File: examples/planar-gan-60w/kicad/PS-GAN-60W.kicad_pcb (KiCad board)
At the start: 8 copper layers, 80 x 58 mm, 89 parts, among them J1 XT30 48V INPUT, J2 XT30 12V OUTPUT, Q1 CSD18543Q3A, Q2 CSD18543Q3A, T1 4:2:2 / Lm 13.12uH, U1 LMG2100R044RARR, U2 UCC25600DR, U3 UCC24624DR, U4 LM5164DDAR, U5 TPS7A2450DBVR, U6 EL357N(A)(TA)-VG, U7 TL431AIDBZR, U8 EL357N(A)(TA)-VG, U9 TL431AIDBZR

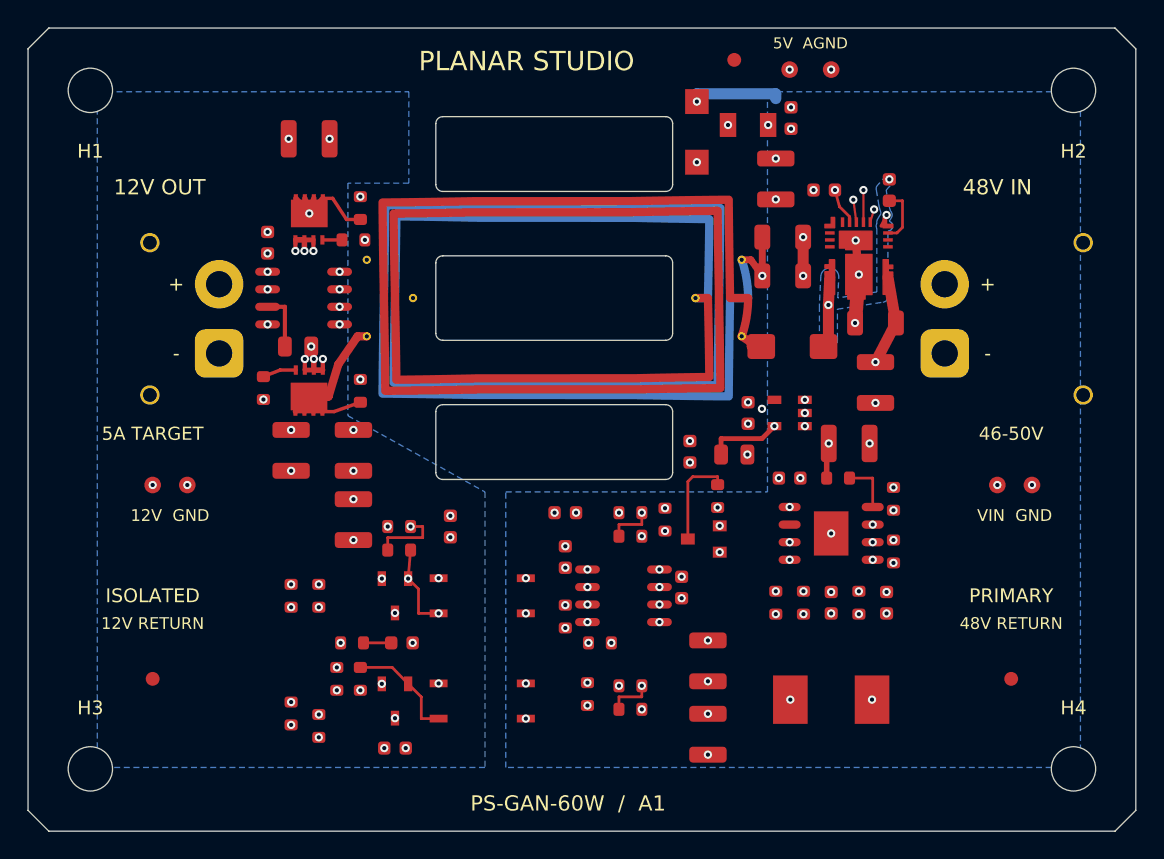
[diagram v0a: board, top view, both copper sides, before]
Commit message: Redraw GaN schematic and compact the bench-accessible A2 board
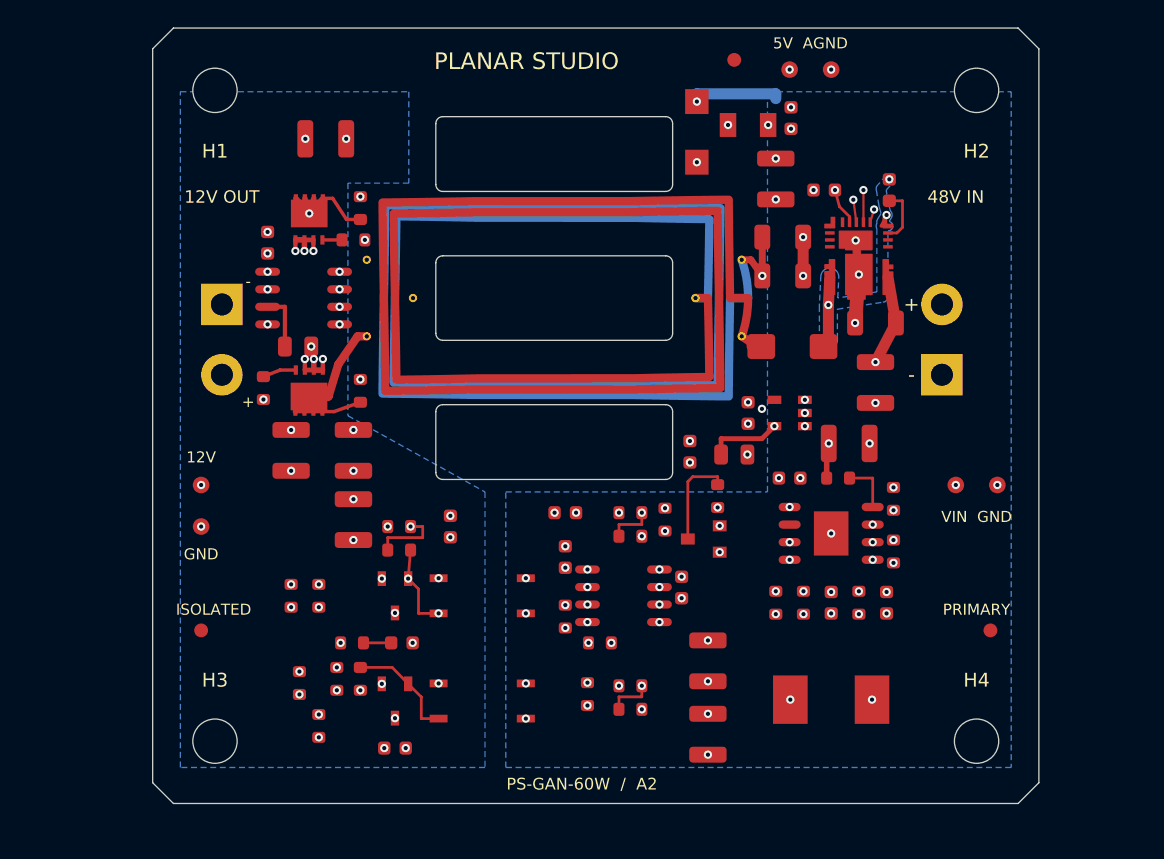
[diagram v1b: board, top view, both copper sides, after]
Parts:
- C7, C8: value 100nF/100V C0G -> 100nF/100V
- D2: value BAT54SLT1G -> BAT54S
- J1: value XT30 48V INPUT -> 48 V INPUT; footprint PS:AMASS_XT30PW-M_1x02_P2.50mm_Horizontal -> PS:CONN-TH_2P-P5.08_WJ2EDGRC-5.08-2P
- J2: value XT30 12V OUTPUT -> 12 V / 5 A; footprint PS:AMASS_XT30PW-F_1x02_P2.50mm_Horizontal -> PS:CONN-TH_2P-P5.08_WJ2EDGRC-5.08-2P
- T1: value 4:2:2 / Lm 13.12uH -> 4 : 2 : 2 / ELP22
- U1: value LMG2100R044RARR -> LMG2100R044
- U2: value UCC25600DR -> UCC25600
- U3: value UCC24624DR -> UCC24624
- U4: value LM5164DDAR -> LM5164
- U5: value TPS7A2450DBVR -> TPS7A2450
- U6, U8: value EL357N(A)(TA)-VG -> EL357N
- U7, U9: value TL431AIDBZR -> TL431A
- moved H3 9.22 mm to (57.5, 107.5)
- moved H1 9.00 mm to (57.5, 60.5)
- moved H4 7.28 mm to (112.5, 107.5)
- moved H2 7.00 mm to (112.5, 60.5)
- moved FID1 4.95 mm to (56.5, 99.5)
- moved FID2 3.81 mm to (113.5, 99.5)
- moved TP3 3.50 mm to (56.5, 89.0)
- moved TP4 3.16 mm to (56.5, 92.0)
- moved TP1 3.00 mm to (111.0, 89.0)
- moved TP2 2.50 mm to (114.0, 89.0)
- moved R27 2.28 mm to (63.6, 103.3)
- moved C15 1.20 mm to (65.5, 64.0)
- moved J1 1.02 mm to (110.0, 78.5), turned to 90 degrees
- moved J2 1.02 mm to (58.0, 78.5), turned to -90 degrees
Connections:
- net /AGND renamed AGND
- net /BIAS12 renamed BIAS12
- net /PGND renamed PGND
- net /SGND renamed SGND
- net /V5 renamed V5
- net /VIN renamed VIN
- net /VOUT renamed VOUT
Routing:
- net VIN: track 103.3 -> 99.7 mm
- net VOUT: track 130.5 -> 128.2 mm
- net /OV_REF: track 17.7 -> 18.3 mm
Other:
- board size 80 x 58 mm -> 64 x 56 mm
- board text added: "12V"
- board text added: "GND"
- board text added: "PS-GAN-60W / A2"
- board text removed: "12V GND"
- board text removed: "12V RETURN"
- board text removed: "46-50V"
- board text removed: "48V RETURN"
- board text removed: "5A TARGET"
- board text removed: "PS-GAN-60W / A1"

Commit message: Improve GaN example schematic spacing and readability
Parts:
- C1, C19, C2: value 2.2uF/100V -> 2.2uF
- C10, C12, C25, C5: value 1uF/25V -> 1uF
- C11, C26: value 2.2uF/25V -> 2.2uF
- C13, C14, C15, C16, C21, C22: value 22uF/25V -> 22uF
- C17, C18, C27, C29: value 10nF/50V -> 10nF
- C20: value 2.2nF/50V -> 2.2nF
- C23: value 3.3nF/50V -> 3.3nF
- C24: value 56pF/50V -> 56pF
- C28: value 1nF/50V -> 1nF
- C3: value 100nF/100V C0G -> 100nF
- C4, C6, C9: value 100nF/50V -> 100nF
- C7, C8: value 100nF/100V -> 100nF
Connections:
- net /BIAS_BST renamed Net-(U4-BST)
- net /BIAS_EN renamed Net-(U4-EN/UVLO)
- net /COMP renamed Net-(C27-Pad1)
- net /CS_AC renamed Net-(C17-Pad2)
- net /CS_RECT renamed Net-(D2-A/C)
- net /DT renamed Net-(U2-DT)
- net /FB_K renamed Net-(U6-CA)
- net /FB_LED renamed Net-(U6-AN)
- net /GD1 renamed Net-(U2-GD1)
- net /GD2 renamed Net-(U2-GD2)
- net /HB renamed Net-(U1-HB)
- net /OV_K renamed Net-(U8-CA)
- net /OV_LED renamed Net-(U8-AN)
- net /OV_REF renamed Net-(U9-REF)
- net /PRI_A renamed Net-(T1-P_DOT)
- net /RIPPLE renamed Net-(C23-Pad1)
- net /RON renamed Net-(U4-RON)
- net /RT renamed Net-(U2-RT)
- net /SR_G1 renamed Net-(Q1-G)
- net /SR_G2 renamed Net-(Q2-G)
- net /SR_REG renamed Net-(U3-REG)
- net /VG1 renamed Net-(U3-VG1)
- net /VG2 renamed Net-(U3-VG2)
- net /VREF renamed Net-(U7-REF)
- net /VS1 renamed Net-(U3-VD1)
- net /VS2 renamed Net-(U3-VD2)

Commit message: Wire sense and bias circuits cohesively in GaN schematic
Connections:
- net /BIAS_FB renamed Net-(U4-FB)
- net /BIAS_SW renamed Net-(U4-SW)
- net /OC renamed Net-(D2-C)
- net /SEC_A renamed Net-(T1-S_DOT)
- net /SEC_B renamed Net-(T1-S_END)

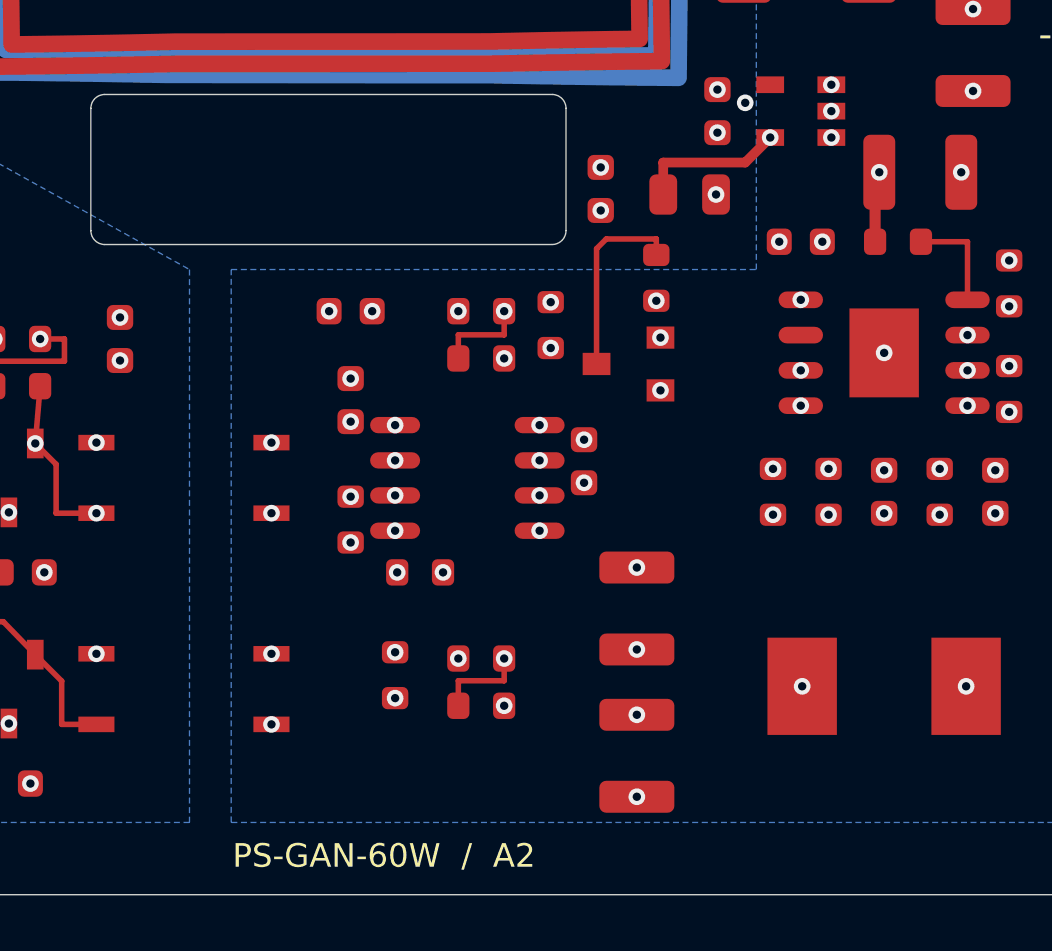
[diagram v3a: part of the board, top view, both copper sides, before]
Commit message: Clarify GaN schematic and correct LM5164 RON grounding
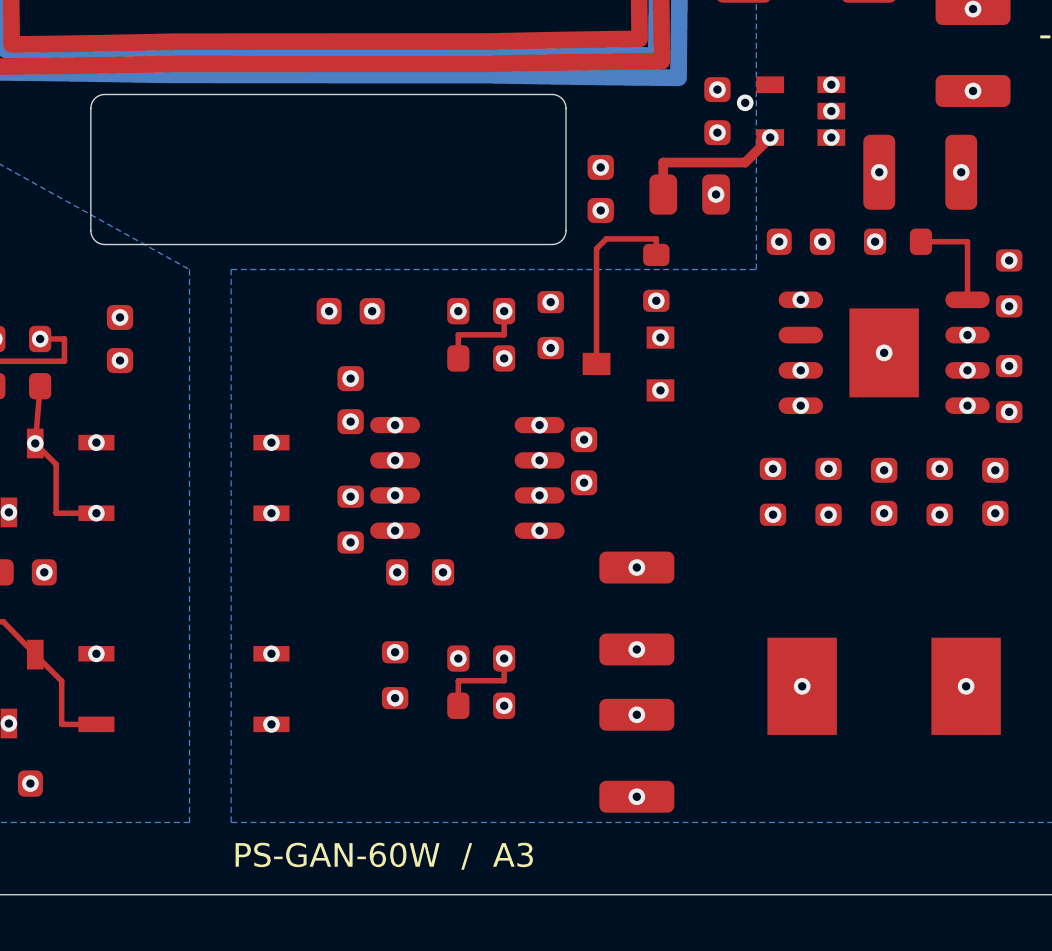
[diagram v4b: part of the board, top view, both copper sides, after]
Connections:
- R16 pad 1: VIN -> PGND
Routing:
- net VIN: track 99.7 -> 97.2 mm
- net PGND: vias 16 -> 17
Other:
- board text added: "PS-GAN-60W / A3"
- board text removed: "PS-GAN-60W / A2"

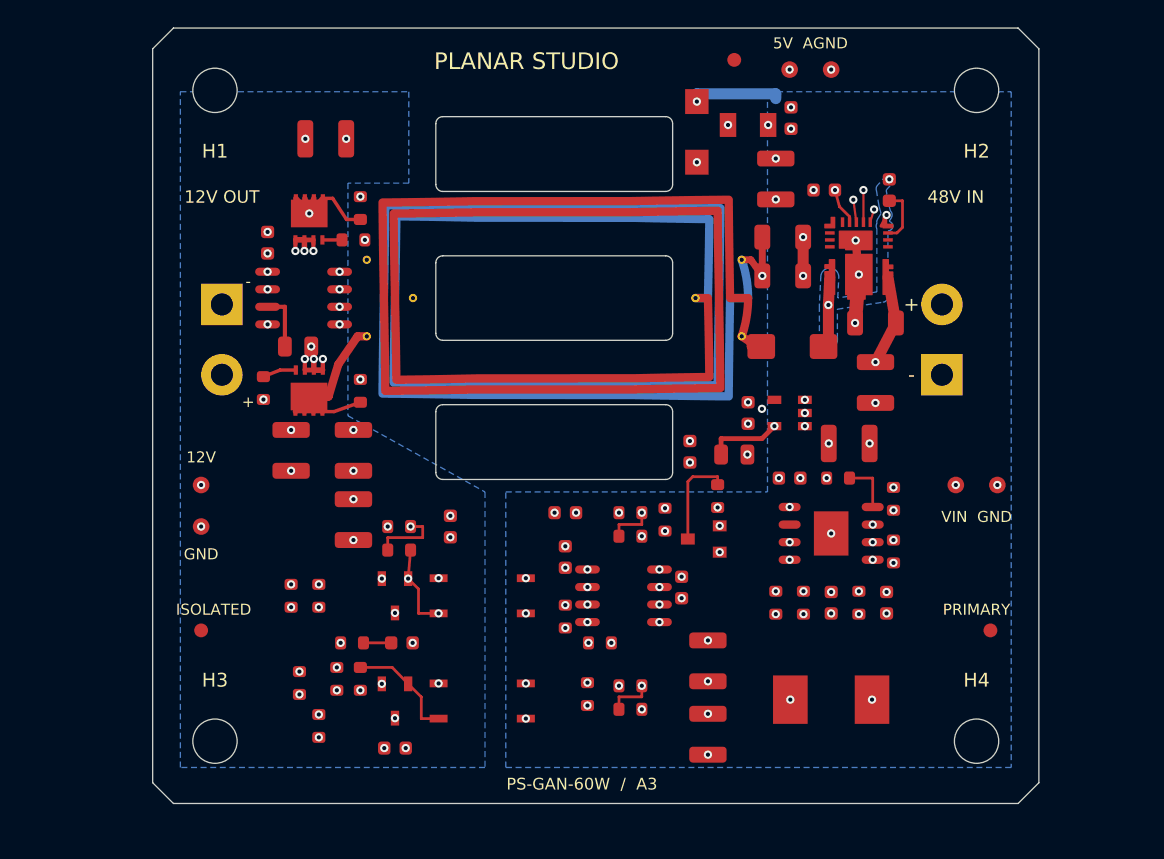
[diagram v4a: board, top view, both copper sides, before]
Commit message: Tighten GaN switching loops and separate rectifier sense return
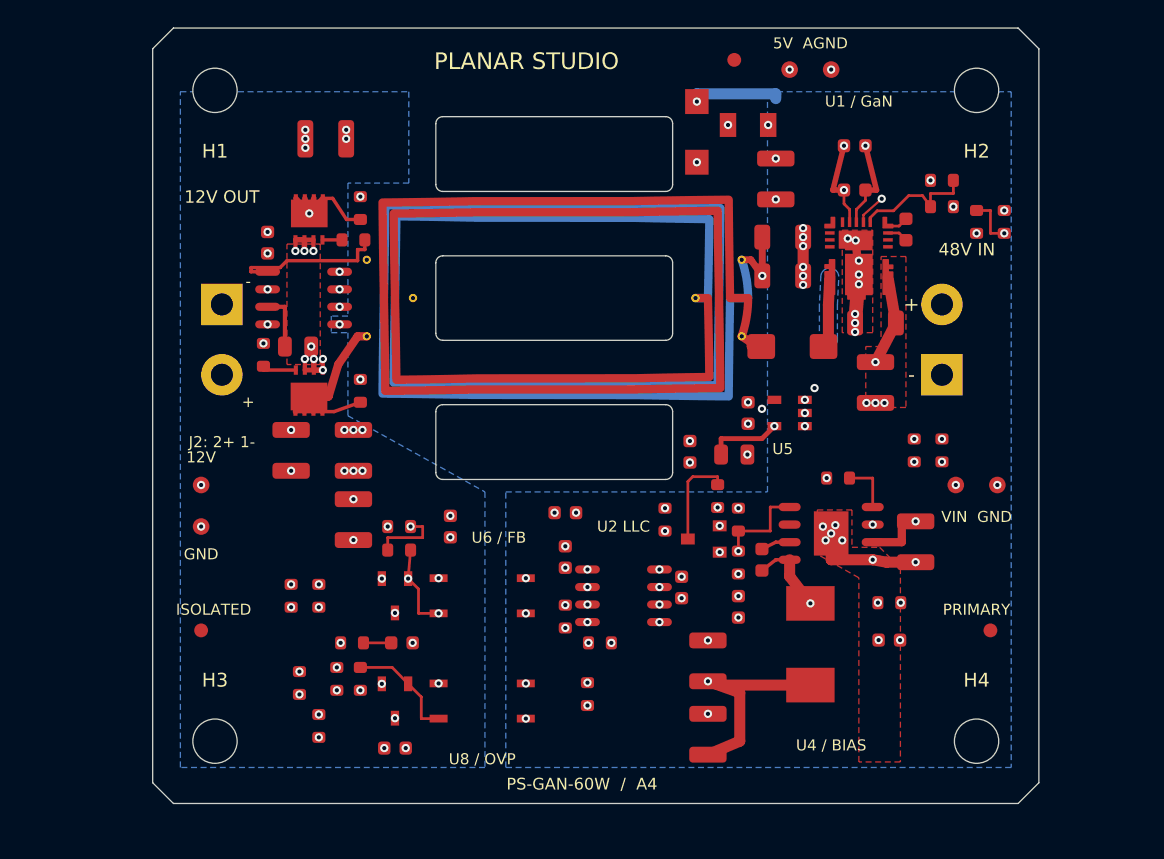
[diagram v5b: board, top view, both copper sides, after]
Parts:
- moved R7 44.4 mm to (114.5, 70.0), turned to 90 degrees
- moved R6 41.8 mm to (112.5, 70.0), turned to 90 degrees
- moved R4 32.9 mm to (110.0, 67.0)
- moved R5 32.8 mm to (110.0, 68.9)
- moved C19 8.57 mm to (108.1, 93.1), turned to -90 degrees
- moved R15 8.10 mm to (110.0, 86.5)
- moved C24 6.71 mm to (95.3, 97.8)
- moved R17 6.58 mm to (95.3, 91.5), turned to -90 degrees
- moved C20 6.23 mm to (97.0, 94.4), turned to -90 degrees
- moved R18 5.52 mm to (95.3, 94.6), turned to -90 degrees
- moved C5 5.02 mm to (103.7, 64.5), turned to 180 degrees
- moved L2 4.27 mm to (100.5, 100.5), turned to -90 degrees
- moved R14 3.81 mm to (108.0, 86.5)
- moved C4 3.09 mm to (107.4, 70.5)
- moved C23 2.71 mm to (106.2, 100.2), turned to 0 degrees
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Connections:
- C4 pad 2: /SW -> Net-(U1-HS)
- U1 pad 11: /SW -> Net-(U1-HS)
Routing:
- net Net-(U2-GD1): track 7.02 -> 55.9 mm
- net Net-(U2-GD2): track 8.37 -> 49.4 mm
- net /LI: track 54.8 -> 19.5 mm
- net /HI: track 41.5 -> 9.30 mm, vias 2 -> 0
- net PGND: track 15.4 -> 34.8 mm, vias 17 -> 32
- net Net-(U4-SW): track 29.6 -> 11.0 mm, vias 4 -> 2
- net /SW: track 19.3 -> 5.13 mm, vias 3 -> 0
- net AGND: track 52.0 -> 62.9 mm
- net /VIN_RAW: track 29.9 -> 40.0 mm
- net Net-(C23-Pad1): track 6.96 -> 16.4 mm
- net VIN: track 97.2 -> 89.9 mm, vias 8 -> 7
- net BIAS12: track 78.5 -> 85.3 mm, vias 10 -> 8
- net SGND: track 10.3 -> 16.5 mm, vias 20 -> 24
- net V5: track 47.7 -> 53.8 mm, vias 5 -> 4
- net Net-(U4-FB): track 16.1 -> 10.8 mm, vias 4 -> 2
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- added copper zone on In1.Cu, net AGND
- added copper zone on F.Cu, net PGND
- added copper zone on F.Cu, net SGND
- added copper zone on In1.Cu, net SGND
- added copper zone on F.Cu, net VIN
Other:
- board text added: "J2: 2+ 1-"
- board text added: "PS-GAN-60W / A4"
- board text added: "U1 / GaN"
- board text added: "U2 LLC"
- board text added: "U4 / BIAS"
- board text added: "U5"
- board text added: "U6 / FB"
- board text added: "U8 / OVP"
- board text removed: "PS-GAN-60W / A3"

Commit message: Refine GaN example return paths and rectifier placement
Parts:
- C10: footprint PS:C_0603_1608Metric -> PS:C_0805_2012Metric
- moved R7 14.6 mm to (99.9, 69.8), turned to 0 degrees
- moved R6 12.8 mm to (99.9, 68.0), turned to 0 degrees
- moved C12 9.27 mm to (64.5, 80.2), turned to 0 degrees
- moved C11 8.19 mm to (61.0, 71.2), turned to 180 degrees
- moved C25 6.54 mm to (102.5, 84.5)
- moved C26 2.75 mm to (96.5, 84.5), turned to 180 degrees
- moved C1 2.72 mm to (99.6, 64.7)
- moved C15 1.40 mm to (65.5, 65.4)
- moved C13 1.20 mm to (63.0, 87.7)
- moved C14 1.20 mm to (67.5, 87.7)
- moved C16 1.20 mm to (67.5, 92.7)
- moved C7 1.12 mm to (98.7, 72.2)
- moved C8 1.12 mm to (98.7, 75.0)
- moved R10 1.08 mm to (66.9, 72.2), turned to 90 degrees
- moved Q2 1.00 mm to (64.3, 83.2)
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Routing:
- net AGND: track 62.9 -> 30.1 mm, vias 19 -> 18
- net Net-(U3-VG1): track 11.4 -> 1.11 mm
- net Net-(U2-GD1): track 55.9 -> 45.9 mm
- net Net-(U2-GD2): track 49.4 -> 40.0 mm
- net Net-(U3-VD1): track 17.1 -> 11.0 mm
- net Net-(U3-VG2): track 11.7 -> 6.08 mm
- net V5: track 53.8 -> 48.5 mm
- net VIN: track 89.9 -> 84.7 mm
- net /LI: track 19.5 -> 14.4 mm
- net VOUT: track 130.8 -> 132.9 mm, vias 15 -> 14
- net Net-(U3-VD2): track 5.87 -> 7.73 mm
- net Net-(U3-REG): track 4.12 -> 2.55 mm
- net Net-(Q2-G): track 2.62 -> 4.17 mm
- net /TANK_C: track 22.2 -> 20.8 mm
- net BIAS12: track 85.3 -> 86.1 mm, vias 8 -> 6
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- added copper zone on In3.Cu, net AGND
- added copper zone on In5.Cu, net AGND
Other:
- board text added: "PS-GAN-60W / A5"
- board text removed: "PS-GAN-60W / A4"

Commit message: Refine GaN layout and add verified ground stitching
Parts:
- moved R25 8.10 mm to (73.9, 100.2), turned to 0 degrees
- moved C18 7.43 mm to (82.1, 98.4), turned to 180 degrees
- moved R1 6.19 mm to (82.1, 95.1), turned to 180 degrees
- moved C9 6.14 mm to (82.1, 100.3), turned to 180 degrees
- moved R26 6.00 mm to (73.9, 101.9), turned to 0 degrees
- moved C28 5.32 mm to (69.7, 94.3), turned to 180 degrees
- moved R9 5.22 mm to (84.9, 92.6)
- moved C16 4.50 mm to (63.0, 92.7)
- moved D2 4.31 mm to (88.5, 92.6), turned to 180 degrees
- moved R22 3.92 mm to (66.7, 95.7)
- moved R20 3.16 mm to (73.9, 92.6)
- moved R21 3.16 mm to (73.9, 94.3)
- moved R27 3.10 mm to (66.7, 103.3)
- moved R3 2.98 mm to (82.1, 102.2), turned to 180 degrees
- moved R23 2.40 mm to (66.7, 98.7)
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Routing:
- net Net-(U7-REF): track 32.1 -> 14.8 mm, vias 5 -> 3
- net Net-(D2-C): track 23.6 -> 9.06 mm, vias 4 -> 2
- net VOUT: track 132.9 -> 145.9 mm
- net V5: track 48.5 -> 61.1 mm
- net Net-(U9-REF): track 18.3 -> 10.9 mm, vias 4 -> 2
- net Net-(U8-AN): track 13.2 -> 7.24 mm, vias 3 -> 2
- net Net-(U4-EN/UVLO): track 11.8 -> 6.97 mm, vias 3 -> 2
- net Net-(U2-DT): track 5.95 -> 1.48 mm, vias 2 -> 0
- net /FB_COL: track 11.2 -> 7.02 mm
- net Net-(D2-A/C): track 7.02 -> 3.12 mm
- net Net-(C17-Pad2): track 9.25 -> 5.67 mm
- net /SS: track 12.2 -> 8.66 mm, vias 3 -> 2
- net Net-(U2-RT): track 10.5 -> 7.55 mm, vias 3 -> 2
- net Net-(U6-AN): track 9.67 -> 7.24 mm
- net Net-(U6-CA): track 22.1 -> 20.8 mm, vias 4 -> 2
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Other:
- board text added: "PS-GAN-60W / A6"
- board text added: "U2 / LLC"
- board text removed: "PS-GAN-60W / A5"
- board text removed: "U2 LLC"

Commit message: Improve GaN bias routing and audit component stress ratings
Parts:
- F1: value 2A / 63V -> 3A / 65V
- R8: value 15kR -> 24.9kR
- moved C23 16.3 mm to (94.6, 88.8)
- moved R19 11.4 mm to (99.5, 88.3)
- moved F1 0.20 mm to (95.8, 63.0)
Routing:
- net BIAS12: track 86.1 -> 95.6 mm, vias 6 -> 5
- net Net-(C23-Pad1): track 16.4 -> 21.5 mm, vias 3 -> 2
- net Net-(U4-SW): track 11.0 -> 12.1 mm
- net SGND: vias 41 -> 42
- net PGND: vias 57 -> 59
- net AGND: vias 28 -> 30
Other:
- board text added: "PS-GAN-60W / A7"
- board text removed: "PS-GAN-60W / A6"
